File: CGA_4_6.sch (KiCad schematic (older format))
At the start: 18 parts, among them U1 74S112, U15 74LS00, U2 74LS74, U22 74LS51, U23 74LS32, U25 74LS00, U26 74S04, U27 74LS51, U28 74LS10, U29 74S04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

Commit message: More sheet 4
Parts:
- added U16, U20: 74LS04, Package_DIP:DIP-14_W7.62mm_LongPads, symbol 74xx:74LS04
- added unit 2 of U22
- added unit 3 of U23
- added unit 4 of U23
- added unit 4 of U29
- added unit 4 of U30
- U30: footprint Package_DIP:DIP-14_W7.62mm_LongPads -> Package_DIP:DIP-14_W10.16mm_LongPads
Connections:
- net C0: now also U22.2
- net GRPH: now also U22.13, U40.5 (Q1), U16.11, U23.13
- net HRES: now also U40.2 (Q0), U16.13
- net ~CPU_MEM_SEL: now also U30.12
- net ~DISPEN_DLY: now also U23.10, U23.12
- net ~GRPH: now also U16.10
- net ~HRES: now also U16.12
- net at U23.5: now also U22.12, U16.4
- net at U15.12: now also U40.12 (Q4), U16.3
- net at U22.8: now also U23.9
- net VIDEO_ENABLE: now reaches U40.10 (Q3)
- net ENABLE_BLINK: now reaches U40.15 (Q5)
- net ENABLE_BLINK: now also U16.5
- net at U40.7 (Q2): now also U16.9, U22.3, U29.9
- new net: U20.5, U22.6
- new net COLOR_SEL: U22.4
- new net MUX_A: U23.8
- new net MUX_B: U23.11
- new net SEL_BLUE: U20.6
- new net ~BW_1: U29.8
- new net ~BW_2: U16.8, U22.5
- new net ~ENABLE_BLINK: U16.6
- new net ~MEMR: U30.13
- new net ~RD_GATE: U30.11

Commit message: Changed footprints, moving components
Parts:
- U1, U40: footprint Package_DIP:DIP-16_W7.62mm_LongPads -> Package_DIP:DIP-16_W7.62mm
- U15, U16, U2, U20, U22, U23, U25, U26, U27, U28, U29, U46, U47, U48, U49, U62, U65: footprint Package_DIP:DIP-14_W7.62mm_LongPads -> Package_DIP:DIP-14_W7.62mm
- U30: footprint Package_DIP:DIP-14_W10.16mm_LongPads -> Package_DIP:DIP-14_W7.62mm

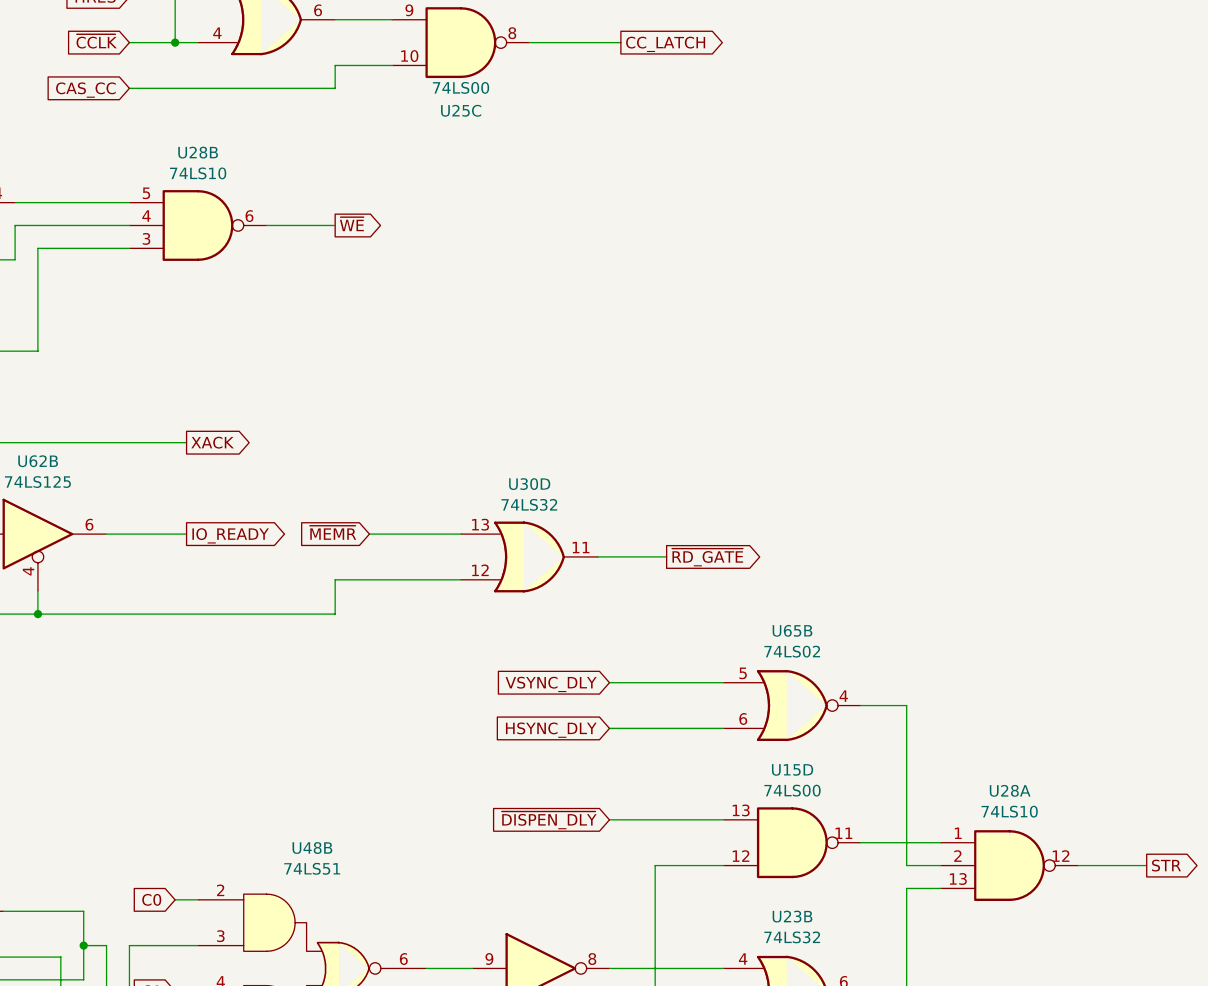
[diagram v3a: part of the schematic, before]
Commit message: Replaced 74LS10 for U28 with 74S10
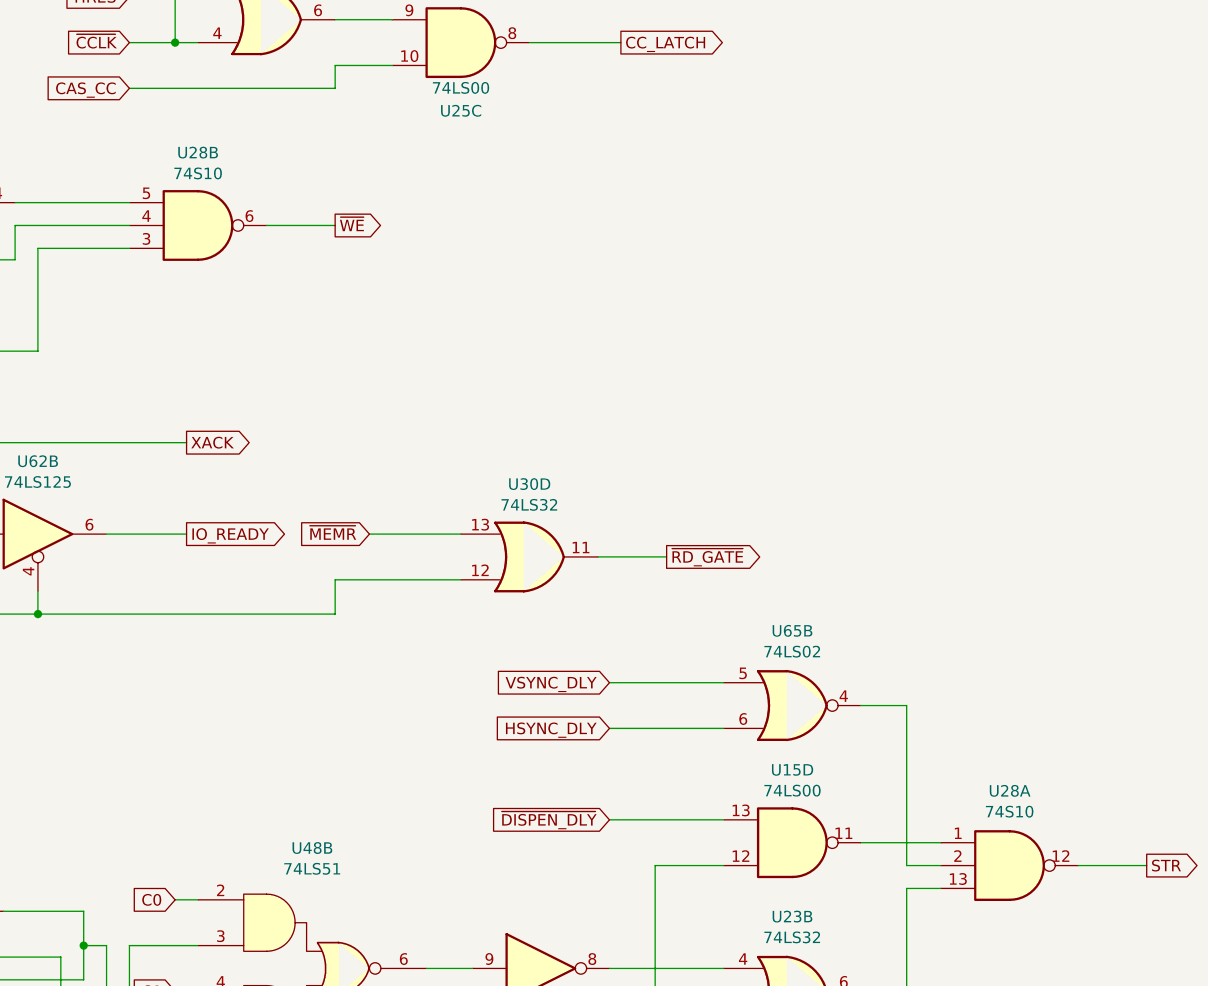
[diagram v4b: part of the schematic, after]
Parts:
- U28: value 74LS10 -> 74S10
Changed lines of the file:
@@
 P 5500 3900
 F 0 "U28" H 5500 3583 50  0000 C CNN
-F 1 "74LS10" H 5500 3674 50  0000 C CNN
+F 1 "74S10" H 5500 3674 50  0000 C CNN
 F 2 "Package_DIP:DIP-14_W7.62mm" H 5500 3900 50  0001 C CNN
 F 3 "http://www.ti.com/lit/gpn/sn74LS10" H 5500 3900 50  0001 C CNN
@@
 AR Path="/60463CC5/63279063" Ref="U28"  Part="1"
 F 0 "U28" H 9050 7025 50  0000 C CNN
-F 1 "74LS10" H 9050 6934 50  0000 C CNN
+F 1 "74S10" H 9050 6934 50  0000 C CNN
 F 2 "Package_DIP:DIP-14_W7.62mm" H 9050 6700 50  0001 C CNN
 F 3 "http://www.ti.com/lit/gpn/sn74LS10" H 9050 6700 50  0001 C CNN

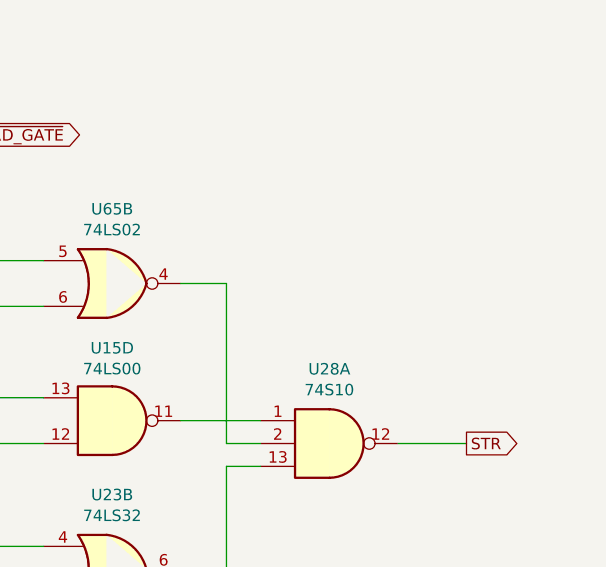
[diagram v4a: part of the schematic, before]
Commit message: Begin working on rev 0.2, for an easier "old" composite out mod
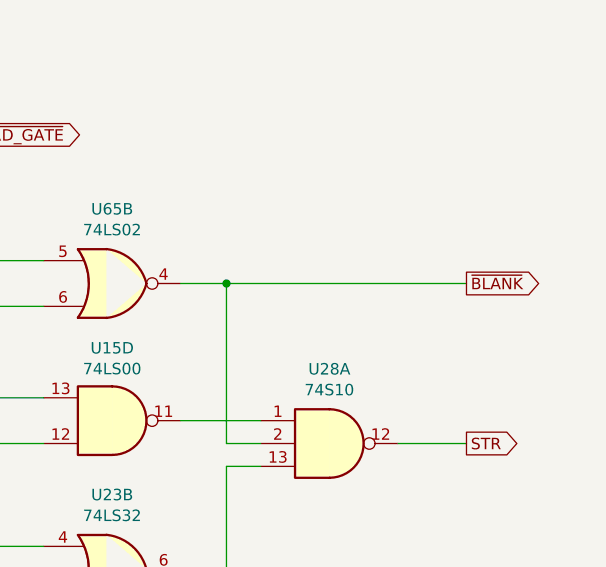
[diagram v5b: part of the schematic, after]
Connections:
- net ~BLANK: now reaches U28.2, U65.4
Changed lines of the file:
@@
 Text GLabel 6700 9700 2    50   Output ~ 0
 GRPH
+Text GLabel 9650 6000 2    50   Output ~ 0
+~BLANK
+Wire Wire Line
+	9650 6000 8600 6000
+Connection ~ 8600 6000
 $EndSCHEMATC
